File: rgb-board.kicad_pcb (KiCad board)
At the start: 2 copper layers, 178 x 129.5 mm, 86 parts, among them J1 Conn_02x25_Odd_Even, J2 SCART-F, J3 TEST_1P, J4 TEST_1P, J5 DE15_Plug_HighDensity_Mountin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, J6 SJ1-3535NG, K1 G6K-2PY-12DC, Q101 BC850C, Q105 BC850C, Q109 BC850C, Q113 BC850C, Q114 BC850C, Q201 BC850C, SW1 SW_DPDT_x2, SW2 SPUJ193700, U1 NCP1117-12_SOT223

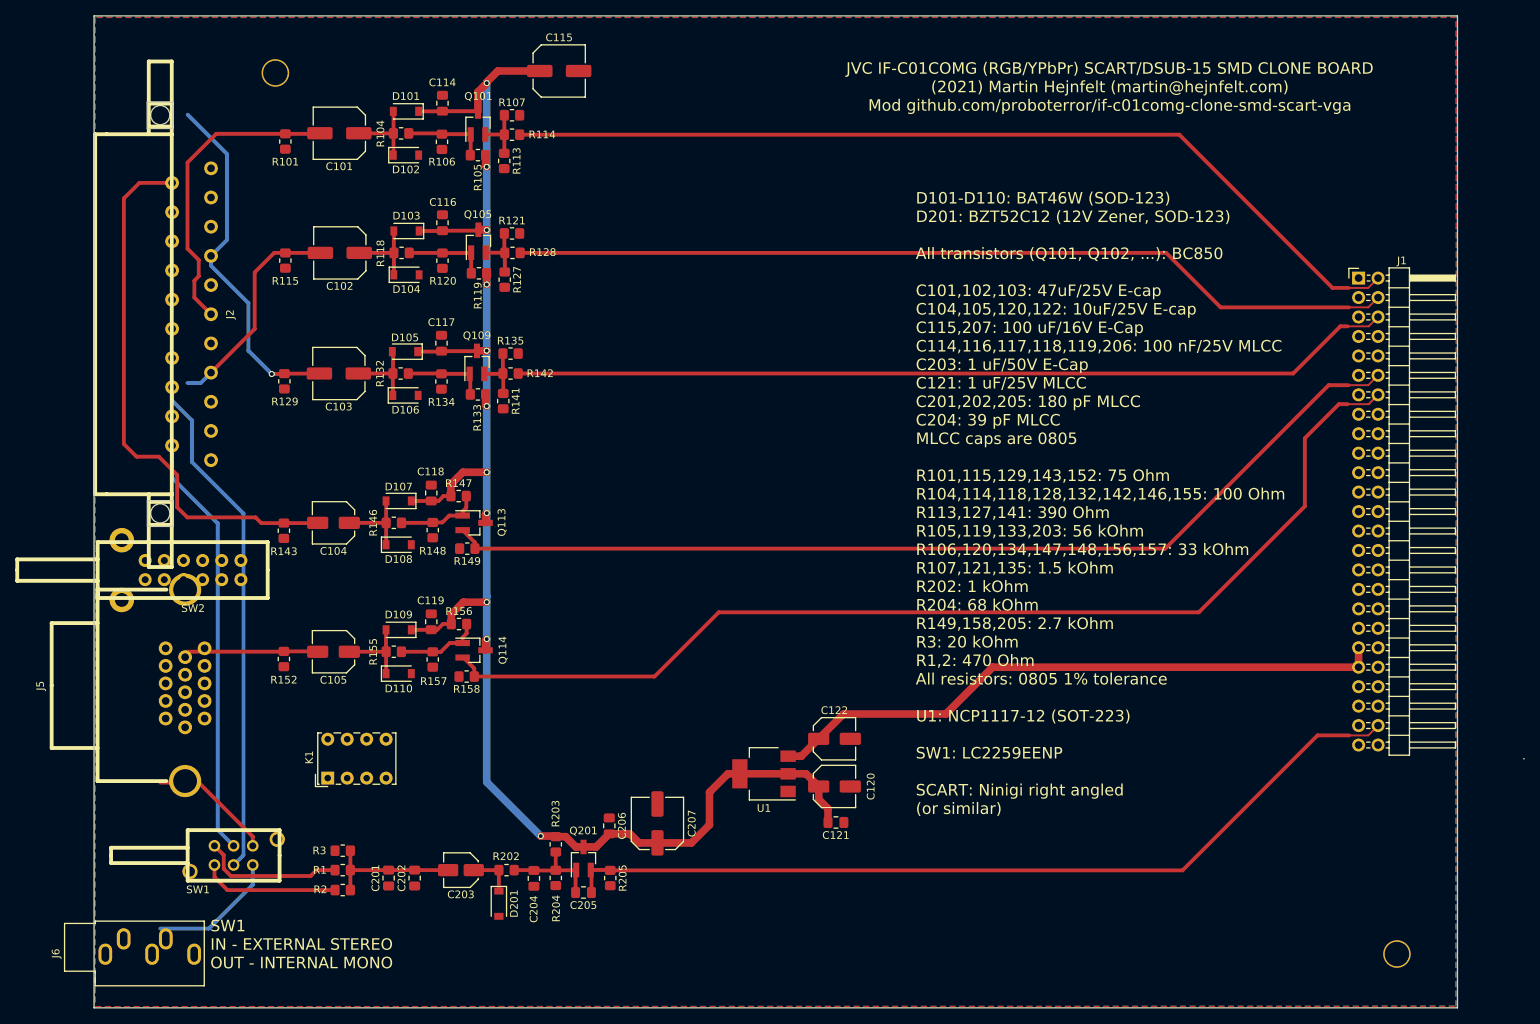
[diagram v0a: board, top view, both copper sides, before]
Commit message: Delete mounting holes / test points.
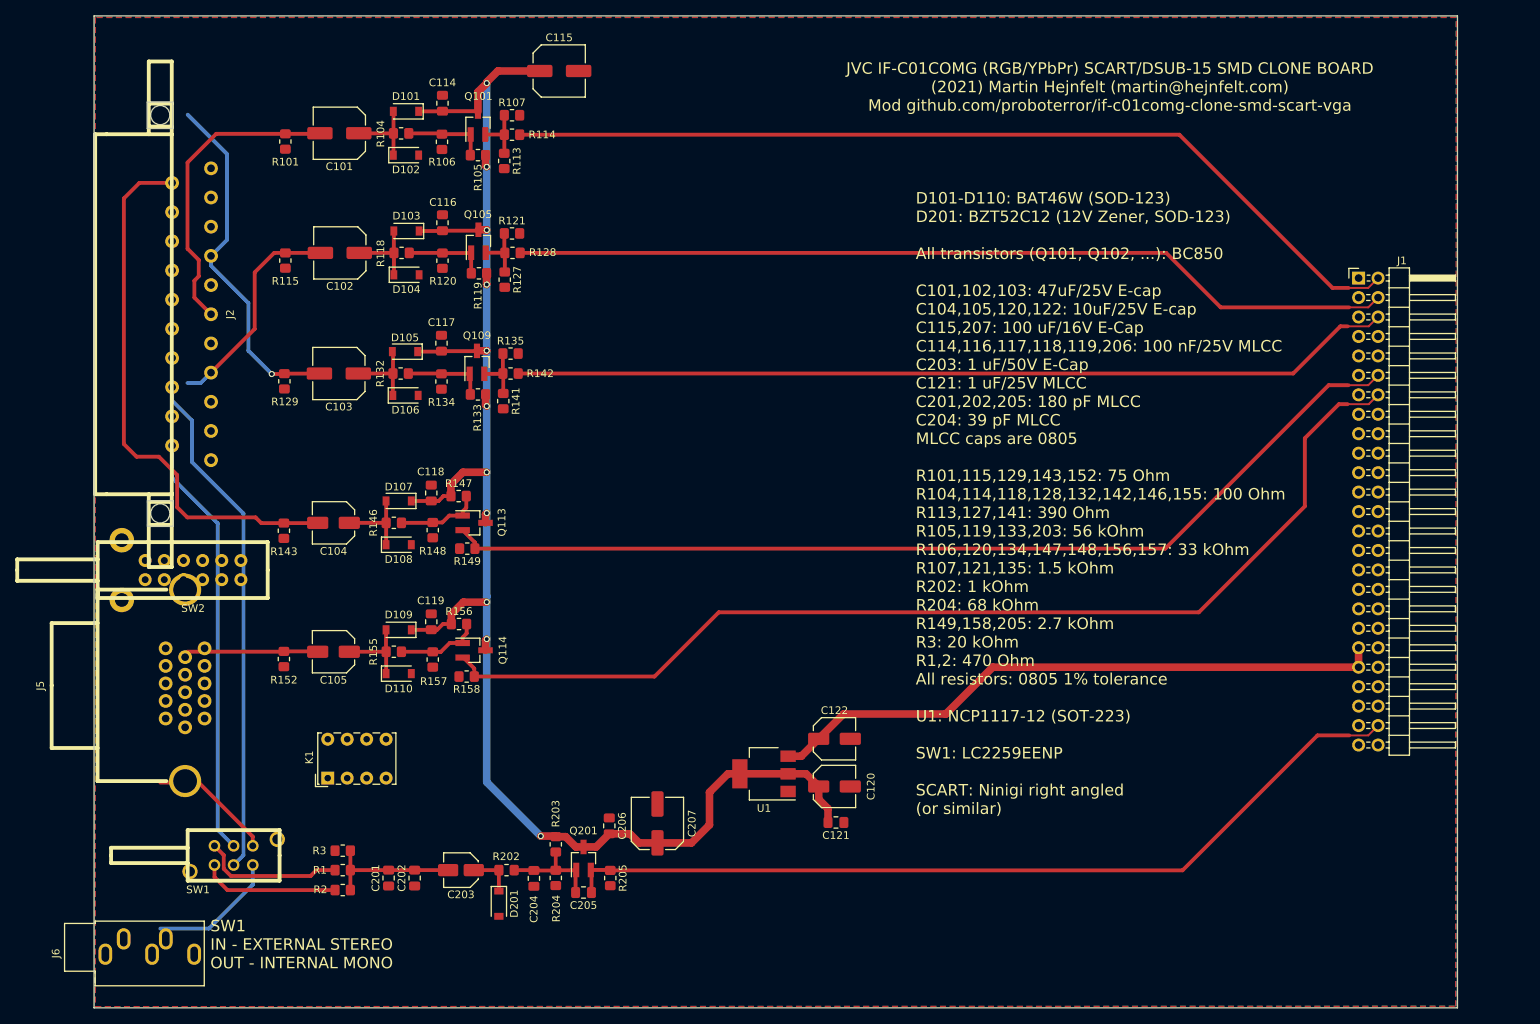
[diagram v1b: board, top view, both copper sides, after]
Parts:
- removed J3, J4: TEST_1P, Mounting_Holes:MountingHole_3.2mm_M3
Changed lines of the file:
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@@
 	(net 104 "unconnected-(K1-Pad5)")
 	(net 105 "unconnected-(K1-Pad8)")
-	(footprint "Mounting_Holes:MountingHole_3.2mm_M3"
-		(layer "F.Cu")
-		(at 73.5 37.85)
-		(descr "Mounting Hole 3.2mm, no annular, M3")
-		(tags "mounting hole 3.2mm no annular m3")
-		(property "Reference" "J3"
-			(at 0 4.55 0)
-			(layer "F.SilkS")
-			(hide yes)
-			(effects
-				(font
-					(size 1 1)
-					(thickness 0.15)
-				)
-			)
-		)
-		(property "Value" "TEST_1P"
-			(at 0 4.2 0)
-			(layer "F.Fab")
-			(effects
-				(font
-					(size 1 1)
-					(thickness 0.15)
-				)
-			)
-		)
-		(property "Footprint" "Mounting_Holes:MountingHole_3.2mm_M3"
-			(at 0 0 0)
-			(unlocked yes)
-			(layer "F.Fab")
-			(hide yes)
-			(effects
-				(font
-					(size 1.27 1.27)
-				)
-			)
-		)
-		(property "Datasheet" ""
-			(at 0 0 0)
-			(unlocked yes)
-			(layer "F.Fab")
-			(hide yes)
-			(effects
-				(font
-					(size 1.27 1.27)
-				)
-			)
-		)
-		(property "Description" ""
-			(at 0 0 0)
-			(unlocked yes)
-			(layer "F.Fab")
-			(hide yes)
-			(effects
-				(font
-					(size 1.27 1.27)
-				)
-			)
-		)
-		(sheetname "Root")
-		(sheetfile "rgb-board.kicad_sch")
-		(zone_connect 2)
-		(attr through_hole)
-		(fp_circle
-			(center 0 0)
-			(end 3.2 0)
-			(stroke
-				(width 0.15)
-				(type solid)
-			)
-			(fill none)
-			(layer "Cmts.User")
-		)
-		(fp_circle
-			(center 0 0)
-			(end 3.45 0)
-			(stroke
-				(width 0.05)
-				(type solid)
-			)
-			(fill none)
-			(layer "F.CrtYd")
-		)
-		(pad "" np_thru_hole circle
-			(at 0 0)
-			(size 3.6 3.6)
-			(drill 3.2)
-			(layers "*.Cu" "*.Mask")
-			(zone_connect 2)
-		)
-	)
-	(footprint "Mounting_Holes:MountingHole_3.2mm_M3"
-		(layer "F.Cu")
-		(at 219.925 152.875)
-		(descr "Mounting Hole 3.2mm, no annular, M3")
-		(tags "mounting hole 3.2mm no annular m3")
-		(property "Reference" "J4"
-			(at 0 -4.2 0)
-			(layer "F.SilkS")
-			(hide yes)
-			(effects
-				(font
-					(size 1 1)
-					(thickness 0.15)
-				)
-			)
-		)
-		(property "Value" "TEST_1P"
-			(at 0 4.2 0)
-			(layer "F.Fab")
-			(effects
-				(font
-					(size 1 1)
-					(thickness 0.15)
-				)
-			)
-		)
-		(property "Footprint" "Mounting_Holes:MountingHole_3.2mm_M3"
-			(at 0 0 0)
-			(unlocked yes)
-			(layer "F.Fab")
-			(hide yes)
-			(effects
-				(font
-					(size 1.27 1.27)
-				)
-			)
-		)
-		(property "Datasheet" ""
-			(at 0 0 0)
-			(unlocked yes)
-			(layer "F.Fab")
-			(hide yes)
-			(effects
-				(font
-					(size 1.27 1.27)
-				)
-			)
-		)
-		(property "Description" ""
-			(at 0 0 0)
-			(unlocked yes)
-			(layer "F.Fab")
-			(hide yes)
-			(effects
-				(font
-					(size 1.27 1.27)
-				)
-			)
-		)
-		(sheetname "Root")
-		(sheetfile "rgb-board.kicad_sch")
-		(zone_connect 2)
-		(attr through_hole)
-		(fp_circle
-			(center 0 0)
-			(end 3.2 0)
-			(stroke
-				(width 0.15)
-				(type solid)
-			)
-			(fill none)
-			(layer "Cmts.User")
-		)
-		(fp_circle
-			(center 0 0)
-			(end 3.45 0)
-			(stroke
-				(width 0.05)
-				(type solid)
-			)
-			(fill none)
-			(layer "F.CrtYd")
-		)
-		(pad "" np_thru_hole circle
-			(at 0 0)
-			(size 3.6 3.6)
-			(drill 3.2)
-			(layers "*.Cu" "*.Mask")
-			(zone_connect 2)
-		)
-	)
 	(footprint "ninigi-scart-ra:NINIGI-SCART-RA"
 		(layer "F.Cu")
@@
 	)
 	(gr_line
-		(start 236.5 127.4)
-		(end 236.5 127.375)
-		(stroke
-			(width 0.2)
-			(type solid)
-		)
-		(layer "F.SilkS")
-	)
-	(gr_line

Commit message: SCART / VGA switching schematic.
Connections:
- J2 pad 11: /G/Y -> /SCART_G
- J2 pad 15: /R/R-Y -> /SCART_R
- J2 pad 20: /HD/CS -> /SCART_SYNC
- J2 pad 7: /B/B-Y -> /SCART_B
- K1 pad 1: unconnected-(K1-Pad1) -> /VGA_SELECT
- K1 pad 2: unconnected-(K1-Pad2) -> /SCART_SYNC
- K1 pad 3: unconnected-(K1-Pad3) -> /HD/CS
- K1 pad 4: unconnected-(K1-Pad4) -> /H_SYNC
- K1 pad 5: unconnected-(K1-Pad5) -> /V_SYNC
- K1 pad 6: unconnected-(K1-Pad6) -> /VD
- K1 pad 8: unconnected-(K1-Pad8) -> GND
- SW2 pad 10: unconnected-(SW2-A4-Pad10) -> /SCART_R
- SW2 pad 11: unconnected-(SW2-COM4-Pad11) -> /R/R-Y
- SW2 pad 12: unconnected-(SW2-B4-Pad12) -> /VGA_R
- SW2 pad 2: unconnected-(SW2-COM1-Pad2) -> /VGA_SELECT
- SW2 pad 3: unconnected-(SW2-B1-Pad3) -> +12V
- SW2 pad 4: unconnected-(SW2-A2-Pad4) -> /SCART_B
- SW2 pad 5: unconnected-(SW2-COM2-Pad5) -> /B/B-Y
- SW2 pad 6: unconnected-(SW2-B2-Pad6) -> /VGA_B
- SW2 pad 7: unconnected-(SW2-A3-Pad7) -> /SCART_G
- SW2 pad 8: unconnected-(SW2-COM3-Pad8) -> /G/Y
- SW2 pad 9: unconnected-(SW2-B3-Pad9) -> /VGA_G
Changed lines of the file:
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@@
 	(net 84 "unconnected-(J5-Pad0)_0")
 	(net 85 "unconnected-(J5-Pad15)")
-	(net 86 "unconnected-(SW2-A4-Pad10)")
-	(net 87 "unconnected-(SW2-COM3-Pad8)")
-	(net 88 "unconnected-(SW2-B1-Pad3)")
-	(net 89 "unconnected-(SW2-A2-Pad4)")
-	(net 90 "unconnected-(SW2-COM1-Pad2)")
-	(net 91 "unconnected-(SW2-A3-Pad7)")
-	(net 92 "unconnected-(SW2-B2-Pad6)")
-	(net 93 "unconnected-(SW2-COM2-Pad5)")
-	(net 94 "unconnected-(SW2-B3-Pad9)")
-	(net 95 "unconnected-(SW2-B4-Pad12)")
-	(net 96 "unconnected-(SW2-A1-Pad1)")
-	(net 97 "unconnected-(SW2-COM4-Pad11)")
-	(net 98 "unconnected-(K1-Pad4)")
-	(net 99 "unconnected-(K1-Pad3)")
-	(net 100 "unconnected-(K1-Pad2)")
-	(net 101 "unconnected-(K1-Pad1)")
-	(net 102 "unconnected-(K1-Pad6)")
-	(net 103 "unconnected-(K1-Pad7)")
-	(net 104 "unconnected-(K1-Pad5)")
-	(net 105 "unconnected-(K1-Pad8)")
+	(net 86 "/SCART_SYNC")
+	(net 87 "/SCART_R")
+	(net 88 "/SCART_B")
+	(net 89 "/SCART_G")
+	(net 90 "/VGA_SELECT")
+	(net 91 "unconnected-(SW2-A1-Pad1)")
+	(net 92 "unconnected-(K1-Pad7)")
 	(footprint "ninigi-scart-ra:NINIGI-SCART-RA"
 		(layer "F.Cu")
@@
 			(layers "*.Cu" "*.Mask")
 			(remove_unused_layers no)
-			(net 4 "/B{slash}B-Y")
+			(net 88 "/SCART_B")
 			(pinfunction "P7")
 			(pintype "passive")
@@
 			(layers "*.Cu" "*.Mask")
 			(remove_unused_layers no)
-			(net 2 "/G{slash}Y")
+			(net 89 "/SCART_G")
 			(pinfunction "P11")
 			(pintype "passive")
@@
 			(layers "*.Cu" "*.Mask")
 			(remove_unused_layers no)
-			(net 5 "/R{slash}R-Y")
+			(net 87 "/SCART_R")
 			(pinfunction "P15")
 			(pintype "passive")
@@
 			(layers "*.Cu" "*.Mask")
 			(remove_unused_layers no)
-			(net 18 "/HD{slash}CS")
+			(net 86 "/SCART_SYNC")
 			(pinfunction "P20")
 			(pintype "passive")
@@
 			(layers "*.Cu" "*.Mask")
 			(remove_unused_layers no)
-			(net 101 "unconnected-(K1-Pad1)")
+			(net 90 "/VGA_SELECT")
 			(pintype "passive")
 		)
@@
 			(layers "*.Cu" "*.Mask")
 			(remove_unused_layers no)
-			(net 100 "unconnected-(K1-Pad2)")
+			(net 86 "/SCART_SYNC")
 			(pintype "passive")
 		)
@@
 			(layers "*.Cu" "*.Mask")
 			(remove_unused_layers no)
-			(net 99 "unconnected-(K1-Pad3)")
+			(net 18 "/HD{slash}CS")
 			(pintype "passive")
 		)
@@
 			(layers "*.Cu" "*.Mask")
 			(remove_unused_layers no)
-			(net 98 "unconnected-(K1-Pad4)")
+			(net 75 "/H_SYNC")
 			(pintype "passive")
 		)
@@
 			(layers "*.Cu" "*.Mask")
 			(remove_unused_layers no)
-			(net 104 "unconnected-(K1-Pad5)")
+			(net 82 "/V_SYNC")
 			(pintype "passive")
 		)
@@
 			(layers "*.Cu" "*.Mask")
 			(remove_unused_layers no)
-			(net 102 "unconnected-(K1-Pad6)")
+			(net 6 "/VD")
 			(pintype "passive")
 		)
@@
 			(layers "*.Cu" "*.Mask")
 			(remove_unused_layers no)
-			(net 103 "unconnected-(K1-Pad7)")
-			(pintype "passive")
+			(net 92 "unconnected-(K1-Pad7)")
+			(pintype "passive+no_connect")
 		)
 		(pad "8" thru_hole circle
@@
 			(layers "*.Cu" "*.Mask")
 			(remove_unused_layers no)
-			(net 105 "unconnected-(K1-Pad8)")
+			(net 7 "GND")
 			(pintype "passive")
 		)
@@
 			(layers "*.Cu" "*.Mask")
 			(remove_unused_layers no)
-			(net 96 "unconnected-(SW2-A1-Pad1)")
+			(net 91 "unconnected-(SW2-A1-Pad1)")
 			(pinfunction "A1")
-			(pintype "bidirectional")
+			(pintype "bidirectional+no_connect")
 		)
 		(pad "2" thru_hole circle
@@
 			(layers "*.Cu" "*.Mask")
 			(remove_unused_layers no)
-			(net 90 "unconnected-(SW2-COM1-Pad2)")
+			(net 90 "/VGA_SELECT")
 			(pinfunction "COM1")
 			(pintype "bidirectional")
@@
 			(layers "*.Cu" "*.Mask")
 			(remove_unused_layers no)
-			(net 88 "unconnected-(SW2-B1-Pad3)")
+			(net 8 "+12V")
 			(pinfunction "B1")
 			(pintype "bidirectional")
@@
 			(layers "*.Cu" "*.Mask")
 			(remove_unused_layers no)
-			(net 89 "unconnected-(SW2-A2-Pad4)")
+			(net 88 "/SCART_B")
 			(pinfunction "A2")
 			(pintype "bidirectional")
@@
 			(layers "*.Cu" "*.Mask")
 			(remove_unused_layers no)
-			(net 93 "unconnected-(SW2-COM2-Pad5)")
+			(net 4 "/B{slash}B-Y")
 			(pinfunction "COM2")
 			(pintype "bidirectional")
@@
 			(layers "*.Cu" "*.Mask")
 			(remove_unused_layers no)
-			(net 92 "unconnected-(SW2-B2-Pad6)")
+			(net 81 "/VGA_B")
 			(pinfunction "B2")
 			(pintype "bidirectional")
@@
 			(layers "*.Cu" "*.Mask")
 			(remove_unused_layers no)
-			(net 91 "unconnected-(SW2-A3-Pad7)")
+			(net 89 "/SCART_G")
 			(pinfunction "A3")
 			(pintype "bidirectional")
@@
 			(layers "*.Cu" "*.Mask")
 			(remove_unused_layers no)
-			(net 87 "unconnected-(SW2-COM3-Pad8)")
+			(net 2 "/G{slash}Y")
 			(pinfunction "COM3")
 			(pintype "bidirectional")
@@
 			(layers "*.Cu" "*.Mask")
 			(remove_unused_layers no)
-			(net 94 "unconnected-(SW2-B3-Pad9)")
+			(net 78 "/VGA_G")
 			(pinfunction "B3")
 			(pintype "bidirectional")
@@
 			(layers "*.Cu" "*.Mask")
 			(remove_unused_layers no)
-			(net 86 "unconnected-(SW2-A4-Pad10)")
+			(net 87 "/SCART_R")
 			(pinfunction "A4")
 			(pintype "bidirectional")
@@
 			(layers "*.Cu" "*.Mask")
 			(remove_unused_layers no)
-			(net 97 "unconnected-(SW2-COM4-Pad11)")
+			(net 5 "/R{slash}R-Y")
 			(pinfunction "COM4")
 			(pintype "bidirectional")
@@
 			(layers "*.Cu" "*.Mask")
 			(remove_unused_layers no)
-			(net 95 "unconnected-(SW2-B4-Pad12)")
+			(net 74 "/VGA_R")
 			(pinfunction "B4")
 			(pintype "bidirectional")
